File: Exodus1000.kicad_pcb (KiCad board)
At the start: 2 copper layers, 81.3 x 132.1 mm, 33 parts, among them J1 ARJ-169, M1 ET60S-02-24-02-X-VP-GP, M2 ET60S-02-24-02-X-VP-GP, M3 ET60S-02-24-02-X-VP-GP, M4 ET60S-02-24-02-X-VP-GP, U1 TM4C1294NCPDTGOOD, U2 93LCxxB, U3 FT232H, Y1 Crystal_GND24, Y2 Crystal

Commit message: added some more stuff
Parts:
- added U4: TUSB4041I, Package_QFP:HTQFP-64-1EP_10x10mm_P0.5mm_EP8x8mm_Mask4.4x4.4mm_ThermalVias, F.Cu at (157.0, 33.5)
- added U5: FSUSB42UMX, Package_DFN_QFN:MLPQ-16-1EP_4x4mm_P0.65mm_EP2.8x2.8mm, F.Cu at (160.0, 54.6)
- moved U2 2.85 mm to (149.9, 44.5)
- moved C15 2.84 mm to (147.9, 52.6)
- moved L1 2.84 mm to (147.9, 51.1)
- moved R4 2.84 mm to (147.9, 48.1)
- moved R5 2.84 mm to (147.9, 49.6)
- moved U3 2.84 mm to (141.2, 47.2)
- moved C12 2.84 mm to (151.0, 52.6)
- moved C14 2.84 mm to (151.0, 51.1)
- moved L2 2.84 mm to (151.0, 49.6)
- moved R3 2.84 mm to (151.0, 48.1)

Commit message: layout stuff
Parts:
- removed U4: TUSB4041I, Package_QFP:HTQFP-64-1EP_10x10mm_P0.5mm_EP8x8mm_Mask4.4x4.4mm_ThermalVias
- removed U5: FSUSB42UMX, Package_DFN_QFN:MLPQ-16-1EP_4x4mm_P0.65mm_EP2.8x2.8mm
- added C17: C_Small, Capacitor_SMD:C_0603_1608Metric, F.Cu at (118.6, 140.7)
- added C18: C_Small, Capacitor_SMD:C_0603_1608Metric, F.Cu at (135.3, 133.9)
- added J2: USB_B, Connector_USB:USB_B_OST_USB-B1HSxx_Horizontal, F.Cu at (87.6, 149.9)
- moved J1 131.2 mm to (128.3, 155.8), turned to 0 degrees
- moved C10 125.5 mm to (113.8, 154.2), turned to 180 degrees
- moved R2 125.5 mm to (116.8, 154.2), turned to 180 degrees
- moved Y2 125.1 mm to (78.2, 139.3), turned to 270 degrees
- moved C8 122.5 mm to (113.8, 152.7), turned to 180 degrees
- moved C2 115.7 mm to (109.7, 146.9)
- moved C1 114.6 mm to (106.0, 146.9)
- moved C7 111.6 mm to (97.5, 137.9), turned to 90 degrees
- moved U2 110.3 mm to (82.5, 131.8), turned to 90 degrees
- moved C9 109.8 mm to (98.3, 140.3), turned to 180 degrees
- moved U3 108.6 mm to (86.4, 141.0), turned to 90 degrees
- moved M3 108.2 mm to (106.7, 38.1), turned to 180 degrees
- moved C5 107.7 mm to (99.2, 137.9), turned to 90 degrees
- moved C16 107.2 mm to (86.2, 127.6), turned to 90 degrees
- moved R4 105.6 mm to (86.2, 133.7), turned to 90 degrees
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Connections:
- J1 pad P2: Net-(J1-PadP2) -> /TM4C129/ETH_TXO_P
- J1 pad P3: Net-(J1-PadP3) -> /TM4C129/ETH_TXO_N
- J1 pad P4: Net-(J1-PadP4) -> /TM4C129/ETH_RXI_P
- J1 pad P5: Net-(J1-PadP5) -> /TM4C129/ETH_RXI_N
- J1 pad SH1: Net-(J1-PadSH1) -> GND
- J1 pad SH2: Net-(J1-PadSH1) -> GND
- J1 pad SH3: Net-(J1-PadSH1) -> GND
- J1 pad SH4: Net-(J1-PadSH1) -> GND
- J1 pad SH5: Net-(J1-PadSH1) -> GND
- J1 pad SH6: Net-(J1-PadSH1) -> GND
- J1 pad U2: Net-(J1-PadU2) -> /TM4C129/USB_D_N
- J1 pad U3: Net-(J1-PadU3) -> /TM4C129/USB_D_P
- J1 pad U4: Net-(J1-PadU4) -> GND
- M1 pad P1-1: Net-(M1-PadP1-1) -> GND
- M1 pad P1-2: Net-(M1-PadP1-2) -> GND
- M1 pad P1-3: Net-(M1-PadP1-3) -> GND
- M1 pad P1-4: Net-(M1-PadP1-4) -> GND
- M1 pad P1-5: Net-(M1-PadP1-5) -> GND
- M1 pad P1-6: Net-(M1-PadP1-6) -> GND
- M1 pad P1-7: Net-(M1-PadP1-7) -> GND
- M1 pad P1-8: Net-(M1-PadP1-8) -> GND
- M1 pad P2-1: Net-(M1-PadP2-1) -> +BATT
- M1 pad P2-2: Net-(M1-PadP2-2) -> +BATT
- M1 pad P2-3: Net-(M1-PadP2-3) -> +BATT
- M1 pad P2-4: Net-(M1-PadP2-4) -> +BATT
- M1 pad P2-5: Net-(M1-PadP2-5) -> +BATT
- M1 pad P2-6: Net-(M1-PadP2-6) -> +BATT
- M1 pad P2-7: Net-(M1-PadP2-7) -> +BATT
- M1 pad P2-8: Net-(M1-PadP2-8) -> +BATT
- M1 pad P3-1: Net-(M1-PadP3-1) -> +5V
- M1 pad P3-2: Net-(M1-PadP3-2) -> +5V
- M1 pad P3-3: Net-(M1-PadP3-3) -> +5V
- M1 pad P3-4: Net-(M1-PadP3-4) -> +5V
- M1 pad P3-5: Net-(M1-PadP3-5) -> +5V
- M1 pad P3-6: Net-(M1-PadP3-6) -> +5V
- M1 pad P3-7: Net-(M1-PadP3-7) -> +5V
- M1 pad P3-8: Net-(M1-PadP3-8) -> +5V
- M1 pad P4-1: Net-(M1-PadP4-1) -> +3V3
- M1 pad P4-2: Net-(M1-PadP4-2) -> +3V3
- M1 pad P4-3: Net-(M1-PadP4-3) -> +3V3
- M1 pad P4-4: Net-(M1-PadP4-4) -> +3V3
- M1 pad P4-5: Net-(M1-PadP4-5) -> +3V3
- M1 pad P4-6: Net-(M1-PadP4-6) -> +3V3
- M1 pad P4-7: Net-(M1-PadP4-7) -> +3V3
- M1 pad P4-8: Net-(M1-PadP4-8) -> +3V3
- M2 pad P1-1: Net-(M2-PadP1-1) -> GND
- M2 pad P1-2: Net-(M2-PadP1-2) -> GND
- M2 pad P1-3: Net-(M2-PadP1-3) -> GND
- M2 pad P1-4: Net-(M2-PadP1-4) -> GND
- M2 pad P1-5: Net-(M2-PadP1-5) -> GND
- M2 pad P1-6: Net-(M2-PadP1-6) -> GND
- M2 pad P1-7: Net-(M2-PadP1-7) -> GND
- M2 pad P1-8: Net-(M2-PadP1-8) -> GND
- M2 pad P2-1: Net-(M2-PadP2-1) -> +BATT
- M2 pad P2-2: Net-(M2-PadP2-2) -> +BATT
- M2 pad P2-3: Net-(M2-PadP2-3) -> +BATT
- M2 pad P2-4: Net-(M2-PadP2-4) -> +BATT
- M2 pad P2-5: Net-(M2-PadP2-5) -> +BATT
- M2 pad P2-6: Net-(M2-PadP2-6) -> +BATT
- M2 pad P2-7: Net-(M2-PadP2-7) -> +BATT
- M2 pad P2-8: Net-(M2-PadP2-8) -> +BATT
- M2 pad P3-1: Net-(M2-PadP3-1) -> +5V
- M2 pad P3-2: Net-(M2-PadP3-2) -> +5V
- M2 pad P3-3: Net-(M2-PadP3-3) -> +5V
- M2 pad P3-4: Net-(M2-PadP3-4) -> +5V
- M2 pad P3-5: Net-(M2-PadP3-5) -> +5V
- M2 pad P3-6: Net-(M2-PadP3-6) -> +5V
- M2 pad P3-7: Net-(M2-PadP3-7) -> +5V
- M2 pad P3-8: Net-(M2-PadP3-8) -> +5V
- M2 pad P4-1: Net-(M2-PadP4-1) -> +3V3
- M2 pad P4-2: Net-(M2-PadP4-2) -> +3V3
- M2 pad P4-3: Net-(M2-PadP4-3) -> +3V3
- M2 pad P4-4: Net-(M2-PadP4-4) -> +3V3
- M2 pad P4-5: Net-(M2-PadP4-5) -> +3V3
- M2 pad P4-6: Net-(M2-PadP4-6) -> +3V3
- M2 pad P4-7: Net-(M2-PadP4-7) -> +3V3
- M2 pad P4-8: Net-(M2-PadP4-8) -> +3V3
- M3 pad P1-1: Net-(M3-PadP1-1) -> GND
- M3 pad P1-2: Net-(M3-PadP1-2) -> GND
- M3 pad P1-3: Net-(M3-PadP1-3) -> GND
- M3 pad P1-4: Net-(M3-PadP1-4) -> GND
- M3 pad P1-5: Net-(M3-PadP1-5) -> GND
- M3 pad P1-6: Net-(M3-PadP1-6) -> GND
- M3 pad P1-7: Net-(M3-PadP1-7) -> GND
- M3 pad P1-8: Net-(M3-PadP1-8) -> GND
- M3 pad P2-1: Net-(M3-PadP2-1) -> +BATT
- M3 pad P2-2: Net-(M3-PadP2-2) -> +BATT
- M3 pad P2-3: Net-(M3-PadP2-3) -> +BATT
- M3 pad P2-4: Net-(M3-PadP2-4) -> +BATT
- M3 pad P2-5: Net-(M3-PadP2-5) -> +BATT
- M3 pad P2-6: Net-(M3-PadP2-6) -> +BATT
- M3 pad P2-7: Net-(M3-PadP2-7) -> +BATT
- M3 pad P2-8: Net-(M3-PadP2-8) -> +BATT
- M3 pad P3-1: Net-(M3-PadP3-1) -> +5V
- M3 pad P3-2: Net-(M3-PadP3-2) -> +5V
- M3 pad P3-3: Net-(M3-PadP3-3) -> +5V
- M3 pad P3-4: Net-(M3-PadP3-4) -> +5V
- M3 pad P3-5: Net-(M3-PadP3-5) -> +5V
- M3 pad P3-6: Net-(M3-PadP3-6) -> +5V
- M3 pad P3-7: Net-(M3-PadP3-7) -> +5V
- M3 pad P3-8: Net-(M3-PadP3-8) -> +5V
- M3 pad P4-1: Net-(M3-PadP4-1) -> +3V3
- M3 pad P4-2: Net-(M3-PadP4-2) -> +3V3
- M3 pad P4-3: Net-(M3-PadP4-3) -> +3V3
- M3 pad P4-4: Net-(M3-PadP4-4) -> +3V3
- M3 pad P4-5: Net-(M3-PadP4-5) -> +3V3
- M3 pad P4-6: Net-(M3-PadP4-6) -> +3V3
- M3 pad P4-7: Net-(M3-PadP4-7) -> +3V3
- M3 pad P4-8: Net-(M3-PadP4-8) -> +3V3
- M4 pad P1-1: Net-(M4-PadP1-1) -> GND
- M4 pad P1-2: Net-(M4-PadP1-2) -> GND
- M4 pad P1-3: Net-(M4-PadP1-3) -> GND
- M4 pad P1-4: Net-(M4-PadP1-4) -> GND
- M4 pad P1-5: Net-(M4-PadP1-5) -> GND
- M4 pad P1-6: Net-(M4-PadP1-6) -> GND
- M4 pad P1-7: Net-(M4-PadP1-7) -> GND
- M4 pad P1-8: Net-(M4-PadP1-8) -> GND
- M4 pad P2-1: Net-(M4-PadP2-1) -> +BATT
- M4 pad P2-2: Net-(M4-PadP2-2) -> +BATT
- M4 pad P2-3: Net-(M4-PadP2-3) -> +BATT
- M4 pad P2-4: Net-(M4-PadP2-4) -> +BATT
- M4 pad P2-5: Net-(M4-PadP2-5) -> +BATT
- M4 pad P2-6: Net-(M4-PadP2-6) -> +BATT
- M4 pad P2-7: Net-(M4-PadP2-7) -> +BATT
- M4 pad P2-8: Net-(M4-PadP2-8) -> +BATT
- M4 pad P3-1: Net-(M4-PadP3-1) -> +5V
- M4 pad P3-2: Net-(M4-PadP3-2) -> +5V
- M4 pad P3-3: Net-(M4-PadP3-3) -> +5V
- M4 pad P3-4: Net-(M4-PadP3-4) -> +5V
- M4 pad P3-5: Net-(M4-PadP3-5) -> +5V
- M4 pad P3-6: Net-(M4-PadP3-6) -> +5V
- M4 pad P3-7: Net-(M4-PadP3-7) -> +5V
- M4 pad P3-8: Net-(M4-PadP3-8) -> +5V
- M4 pad P4-1: Net-(M4-PadP4-1) -> +3V3
- M4 pad P4-2: Net-(M4-PadP4-2) -> +3V3
- M4 pad P4-3: Net-(M4-PadP4-3) -> +3V3
- M4 pad P4-4: Net-(M4-PadP4-4) -> +3V3
- M4 pad P4-5: Net-(M4-PadP4-5) -> +3V3
- M4 pad P4-6: Net-(M4-PadP4-6) -> +3V3
- M4 pad P4-7: Net-(M4-PadP4-7) -> +3V3
- M4 pad P4-8: Net-(M4-PadP4-8) -> +3V3
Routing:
- net /TM4C129/ETH_TXO_P: track 0.00 -> 18.0 mm
- net /TM4C129/ETH_TXO_N: track 0.00 -> 16.7 mm
- net /TM4C129/ETH_RXI_P: track 0.00 -> 13.0 mm
- net /TM4C129/ETH_RXI_N: track 0.00 -> 11.8 mm
- net GND: track 0.00 -> 9.88 mm, vias 0 -> 4
- net Net-(C18-Pad2): track 0.00 -> 8.73 mm
- net /ft232h/D+: track 0.00 -> 8.05 mm
- net +3V3: track 0.00 -> 7.66 mm
- net /TM4C129/OSC0: track 0.00 -> 7.54 mm
- net Net-(C5-Pad1): track 0.00 -> 5.83 mm
- net /ft232h/D-: track 0.00 -> 5.28 mm
- net Net-(C17-Pad2): track 0.00 -> 4.56 mm
- net Net-(C4-Pad2): track 0.00 -> 4.40 mm
- net /TM4C129/OSC1: track 0.00 -> 4.23 mm
- added copper zone on F.Cu, net +3V3
- added copper zone on F.Cu, net +5V
- added copper zone on In1.Cu, net +BATT
- added copper zone on In2.Cu, net GND
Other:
- board size 81.3 x 132.1 mm -> 63.5 x 129.5 mm
- copper layers 2 -> 4
- rule trace_min: 0.2 -> 0.127
- rule via_min_drill: 0.3 -> 0.254
- rule via_min_size: 0.4 -> 0.508

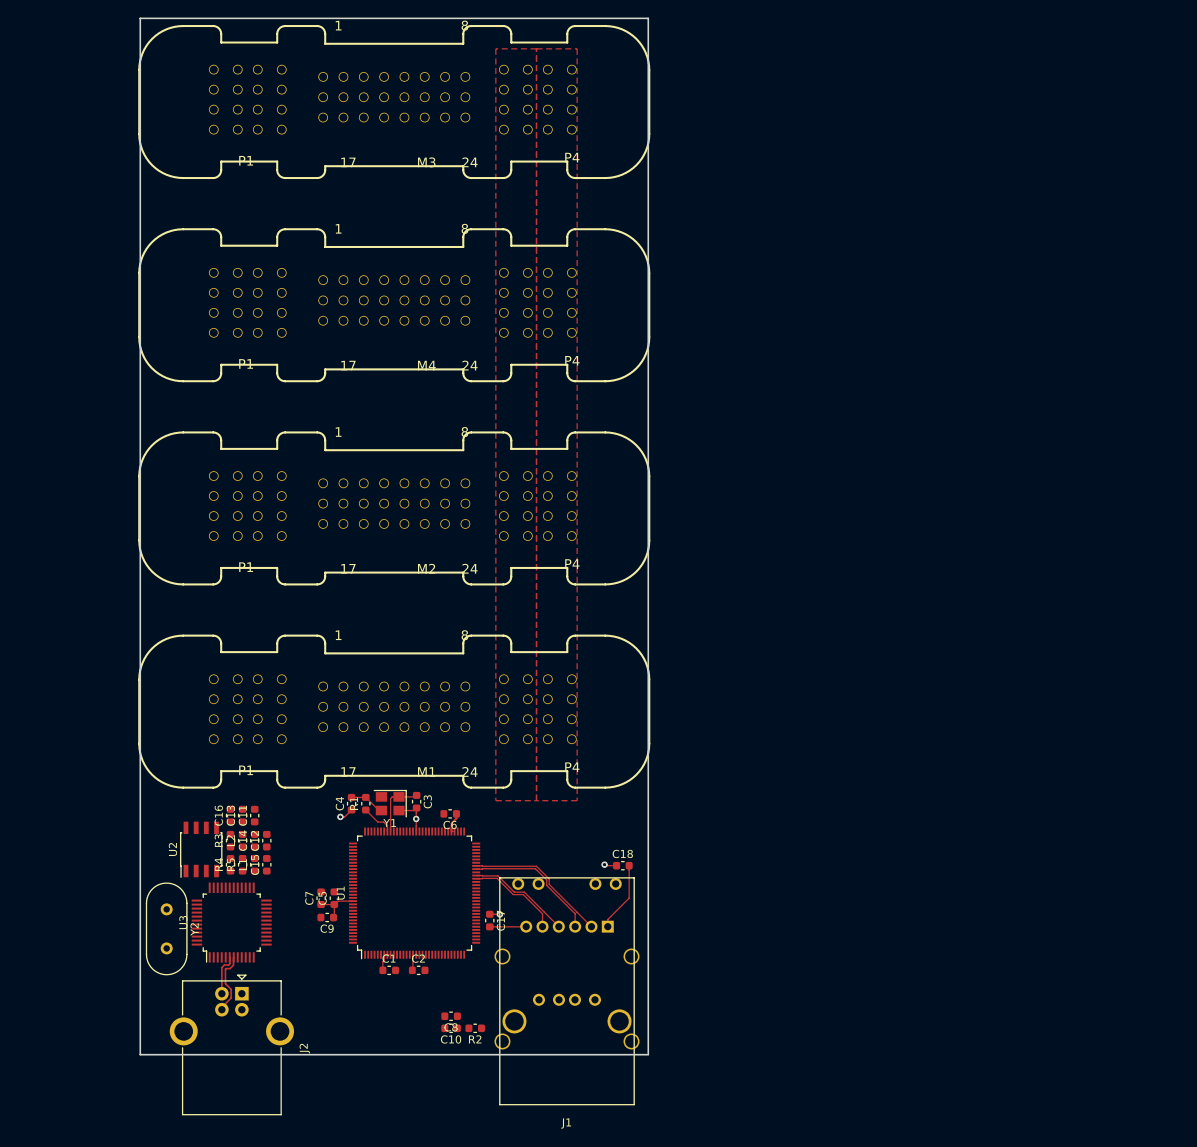
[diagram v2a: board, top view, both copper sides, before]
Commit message: usb hub and sdram selected.
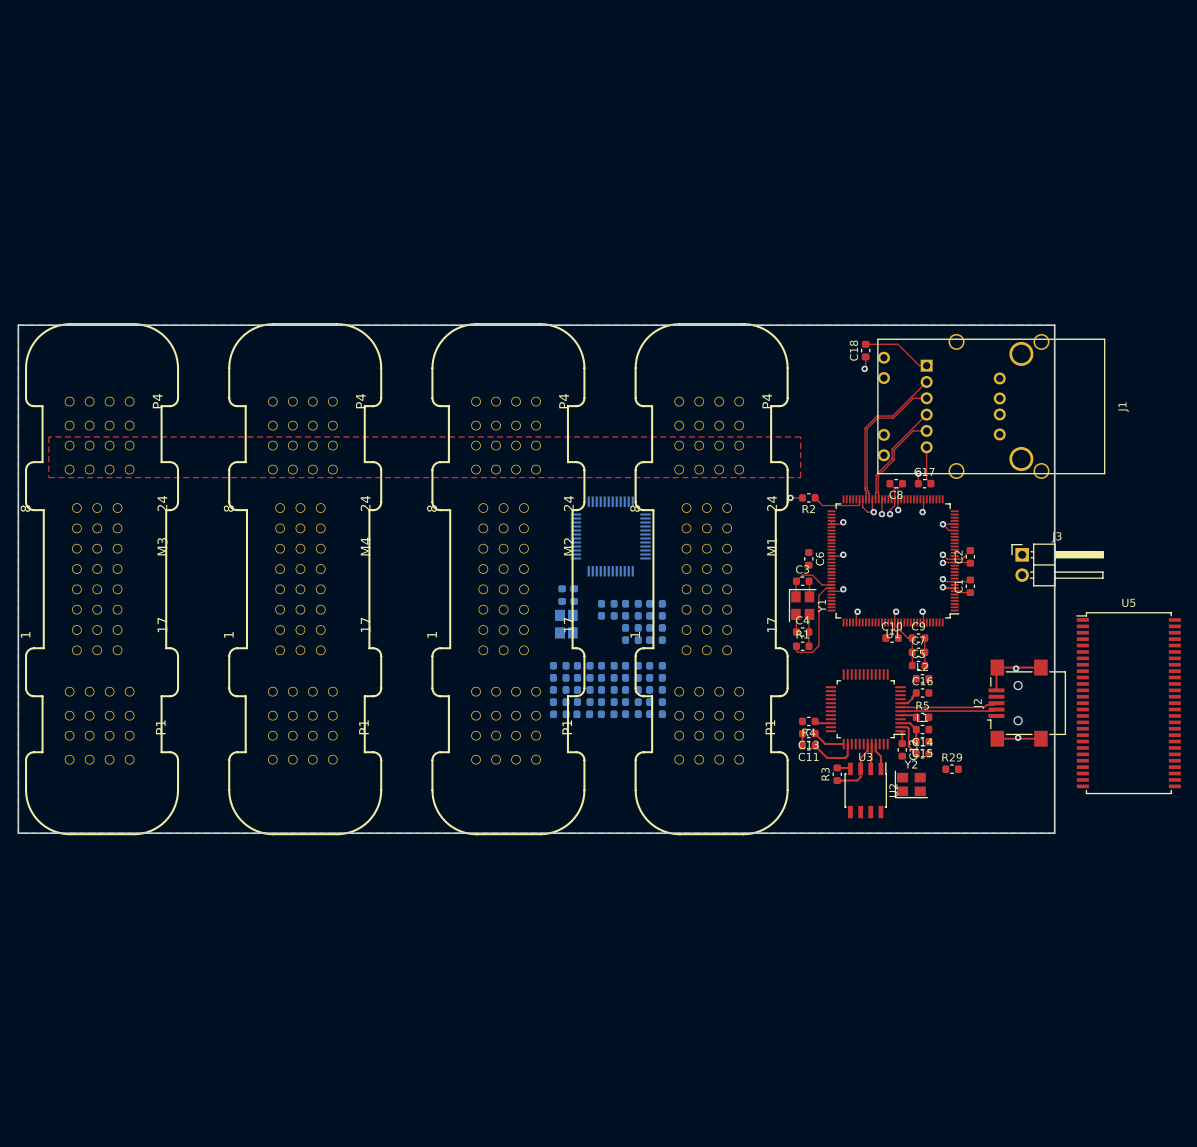
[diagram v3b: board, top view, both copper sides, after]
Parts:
- added C19: C_Small, Capacitor_SMD:C_0603_1608Metric, B.Cu at (127.4, 114.9)
- added C20: C_Small, Capacitor_SMD:C_0603_1608Metric, B.Cu at (127.4, 113.4)
- added C21: C_Small, Capacitor_SMD:C_0603_1608Metric, B.Cu at (130.3, 114.9)
- added C22: C_Small, Capacitor_SMD:C_0603_1608Metric, B.Cu at (127.4, 111.9)
- added C23: C_Small, Capacitor_SMD:C_0603_1608Metric, B.Cu at (130.4, 113.4)
- added C24: C_Small, Capacitor_SMD:C_0603_1608Metric, B.Cu at (133.3, 114.9)
- added C25: C_Small, Capacitor_SMD:C_0603_1608Metric, B.Cu at (127.4, 110.4)
- added C26: C_Small, Capacitor_SMD:C_0603_1608Metric, B.Cu at (130.4, 111.9)
- added C27: C_Small, Capacitor_SMD:C_0603_1608Metric, B.Cu at (133.4, 113.4)
- added C28: C_Small, Capacitor_SMD:C_0603_1608Metric, B.Cu at (127.4, 108.9)
- added C29: C_Small, Capacitor_SMD:C_0603_1608Metric, B.Cu at (136.4, 114.9)
- added C30: C_Small, Capacitor_SMD:C_0603_1608Metric, B.Cu at (139.4, 108.9)
- added C31: C_Small, Capacitor_SMD:C_0603_1608Metric, B.Cu at (127.7, 100.0)
- added C32: C_Small, Capacitor_SMD:C_0603_1608Metric, B.Cu at (129.2, 100.0)
- added J3: Conn_01x02, Connector_PinHeader_2.54mm:PinHeader_1x02_P2.54mm_Horizontal, F.Cu at (185.2, 95.0)
- added R10: R_Small, Resistor_SMD:R_0603_1608Metric, B.Cu at (130.4, 108.9)
- added R11: R_Small, Resistor_SMD:R_0603_1608Metric, B.Cu at (136.4, 111.9)
- added R12: R_Small, Resistor_SMD:R_0603_1608Metric, B.Cu at (139.4, 113.4)
- added R13: R_Small, Resistor_SMD:R_0603_1608Metric, B.Cu at (139.4, 110.4)
- added R14: R_Small, Resistor_SMD:R_0603_1608Metric, B.Cu at (133.4, 108.9)
- added R15: R_Small, Resistor_SMD:R_0603_1608Metric, B.Cu at (136.4, 110.4)
- added R16: R_Small, Resistor_SMD:R_0603_1608Metric, B.Cu at (139.4, 111.9)
- added R17: R_Small, Resistor_SMD:R_0603_1608Metric, B.Cu at (136.4, 108.9)
- added R18: R_Small, Resistor_SMD:R_0603_1608Metric, B.Cu at (133.4, 111.9)
- added R19: R_Small, Resistor_SMD:R_0603_1608Metric, B.Cu at (136.4, 105.7)
- added R20: R_Small, Resistor_SMD:R_0603_1608Metric, B.Cu at (133.4, 102.6)
- added R21: R_Small, Resistor_SMD:R_0603_1608Metric, B.Cu at (136.4, 104.1)
- added R22: R_Small, Resistor_SMD:R_0603_1608Metric, B.Cu at (139.4, 105.7)
- added R23: R_Small, Resistor_SMD:R_0603_1608Metric, B.Cu at (133.4, 101.1)
- added R24: R_Small, Resistor_SMD:R_0603_1608Metric, B.Cu at (136.4, 102.6)
- added R25: R_Small, Resistor_SMD:R_0603_1608Metric, B.Cu at (139.4, 104.1)
- added R26: R_Small, Resistor_SMD:R_0603_1608Metric, B.Cu at (136.4, 101.1)
- added R27: R_Small, Resistor_SMD:R_0603_1608Metric, B.Cu at (139.4, 102.6)
- added R28: R_Small, Resistor_SMD:R_0603_1608Metric, B.Cu at (139.4, 101.1)
- added R29: R_Small, Resistor_SMD:R_0603_1608Metric, F.Cu at (176.4, 121.8)
- added R6: R_Small, Resistor_SMD:R_0603_1608Metric, B.Cu at (130.4, 110.4)
- added R7: R_Small, Resistor_SMD:R_0603_1608Metric, B.Cu at (139.4, 114.9)
- added R8: R_Small, Resistor_SMD:R_0603_1608Metric, B.Cu at (136.4, 113.4)
- added R9: R_Small, Resistor_SMD:R_0603_1608Metric, B.Cu at (133.4, 110.4)
- added U4: tusb2077a, Package_QFP:TQFP-48_7x7mm_P0.5mm, B.Cu at (133.7, 92.7)
- added U5: IS42S16400J-xT, Package_SO:TSOP-II-54_22.2x10.16mm_P0.8mm, F.Cu at (198.5, 113.5)
- added Y3: Crystal_GND24, Crystal:Crystal_SMD_SeikoEpson_FA238-4Pin_3.2x2.5mm, B.Cu at (128.2, 103.7)
- J2: value USB_B -> USB_B_Mini; footprint Connector_USB:USB_B_OST_USB-B1HSxx_Horizontal -> Connector_USB:USB_Mini-B_Lumberg_2486_01_Horizontal
- Y2: value Crystal -> Crystal_GND24; footprint Crystal:Crystal_HC49-4H_Vertical -> Crystal:Crystal_SMD_3225-4Pin_3.2x2.5mm
- moved J2 103.6 mm to (184.7, 113.5), turned to 90 degrees
- moved J1 99.1 mm to (187.6, 76.5), turned to 90 degrees
- moved Y2 94.4 mm to (171.3, 123.7), turned to 0 degrees
- moved C16 87.9 mm to (172.7, 112.3), turned to 0 degrees
- moved L2 87.4 mm to (172.7, 110.5), turned to 0 degrees
- moved C1 87.1 mm to (178.7, 98.9), turned to 90 degrees
- moved R5 87.0 mm to (172.7, 115.3), turned to 0 degrees
- moved C8 86.8 mm to (169.4, 86.1)
- moved C2 86.2 mm to (178.7, 95.2), turned to 90 degrees
- moved L1 85.2 mm to (172.7, 116.8), turned to 0 degrees
- moved C14 84.2 mm to (172.7, 119.9), turned to 0 degrees
- moved U3 83.6 mm to (165.6, 114.3), turned to 180 degrees
- moved C15 83.4 mm to (172.7, 118.4), turned to 180 degrees
- moved U2 83.4 mm to (165.6, 124.5), turned to 270 degrees
- moved C9 81.7 mm to (172.2, 105.4), turned to 0 degrees
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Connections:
- net /TM4C129/JTAG_TCK renamed /JTAG_TCK
- net /TM4C129/JTAG_TDI renamed /JTAG_TDI
- net /TM4C129/JTAG_TDO renamed /JTAG_TDO
- net /TM4C129/JTAG_TMS renamed /JTAG_TMS
- net /ft232h/ACBUS0 renamed /Connectors/sheet5C96EC1B/ACBUS0
- net /ft232h/ACBUS1 renamed /Connectors/sheet5C96EC1B/ACBUS1
- net /ft232h/ACBUS2 renamed /Connectors/sheet5C96EC1B/ACBUS2
- net /ft232h/ACBUS3 renamed /Connectors/sheet5C96EC1B/ACBUS3
- net /ft232h/ACBUS4 renamed /Connectors/sheet5C96EC1B/ACBUS4
- net /ft232h/ACBUS5 renamed /Connectors/sheet5C96EC1B/ACBUS5
- net /ft232h/ACBUS6 renamed /Connectors/sheet5C96EC1B/ACBUS6
- net /ft232h/ACBUS7 renamed /Connectors/sheet5C96EC1B/ACBUS7
- net /ft232h/ACBUS8 renamed /Connectors/sheet5C96EC1B/ACBUS8
- net /ft232h/ACBUS9 renamed /Connectors/sheet5C96EC1B/ACBUS9
- net /ft232h/ADBUS0 renamed /Connectors/JTAG_TCK
- net /ft232h/ADBUS1 renamed /Connectors/JTAG_TDI
- net /ft232h/ADBUS2 renamed /Connectors/JTAG_TDO
- net /ft232h/ADBUS3 renamed /Connectors/JTAG_TMS
- net /ft232h/ADBUS4 renamed /Connectors/~JTAG_TRST
- net /ft232h/ADBUS5 renamed /Connectors/sheet5C96EC1B/ADBUS5
- net /ft232h/ADBUS6 renamed /Connectors/sheet5C96EC1B/ADBUS6
- net /ft232h/ADBUS7 renamed /Connectors/sheet5C96EC1B/ADBUS7
- net /ft232h/D+ renamed /Connectors/sheet5C96EC1B/D+
- net /ft232h/D- renamed /Connectors/sheet5C96EC1B/D-
- J1 pad U2: /TM4C129/USB_D_N -> Net-(J1-PadU2)
- J1 pad U3: /TM4C129/USB_D_P -> Net-(J1-PadU3)
- J2 pad 4: GND -> Net-(J2-Pad4)
- R4 pad 2: +3V3 -> Net-(C14-Pad1)
- R5 pad 2: GND -> +3V3
- U3 pad 2: Net-(C14-Pad1) -> Net-(R4-Pad1)
- U3 pad 34: Net-(R4-Pad1) -> Net-(R5-Pad1)
- U3 pad 5: Net-(R5-Pad1) -> Net-(R29-Pad1)
- Y2 pad 1: Net-(C12-Pad1) -> GND
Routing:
- net GND: track 9.88 -> 45.8 mm, vias 4 -> 9
- net +3V3: track 7.66 -> 30.3 mm, vias 0 -> 12
- net /TM4C129/OSC1: track 4.23 -> 12.0 mm
- net Net-(R3-Pad1): track 0.00 -> 7.60 mm
- net /Connectors/sheet5C96EC1B/D-: track 5.28 -> 12.1 mm
- net Net-(R2-Pad1): track 0.00 -> 6.65 mm
- net +1V8: track 0.00 -> 6.28 mm
- net Net-(C14-Pad1): track 0.00 -> 4.66 mm
- net /Connectors/sheet5C96EC1B/D+: track 8.05 -> 12.2 mm
- net Net-(C13-Pad1): track 0.00 -> 4.11 mm
- net Net-(C15-Pad2): track 0.00 -> 3.83 mm
- net Net-(U2-Pad1): track 0.00 -> 3.38 mm
- net Net-(U2-Pad2): track 0.00 -> 3.16 mm
- net Net-(C16-Pad1): track 0.00 -> 2.63 mm
- net Net-(R5-Pad1): track 0.00 -> 2.08 mm
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- added copper zone on B.Cu, net +3V3
- removed copper zone on F.Cu, net +3V3
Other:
- board size 63.5 x 129.5 mm -> 129.5 x 63.5 mm
